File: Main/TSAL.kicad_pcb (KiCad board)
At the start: 2 copper layers, 140 x 70 mm, 81 parts, among them J1 Mini-SPOX, J2 Mini-SPOX, J3 Mini-Fit_Jr, J4 Mini-SPOX, J5 Mini-SPOX, J6 Jumper, J7 Jumper, Q1 IRLML2502, Q2 IRLML2502, Q3 IRLML2502, Q4 IRLML2502, Q5 IRF8721, U1 74HC08, U2 74HC08, U3 TLV70033, U4 LMC555, U5 LMR14030, U6 ZLDO1117G50, U7 TPS62205, U8 MAX40200AUK

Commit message: Main board: Rev B schematics design
major redesign of power delivery and backup
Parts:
- moved C1 28.3 mm to (187.0, 107.0)
- moved C10 28.3 mm to (118.0, 76.0)
- moved C11 28.3 mm to (129.0, 86.0)
- moved C12 28.3 mm to (120.5, 76.0)
- moved C13 28.3 mm to (199.0, 116.0)
- moved C14 28.3 mm to (144.0, 80.0)
- moved C15 28.3 mm to (205.0, 106.0)
- moved C16 28.3 mm to (201.0, 66.0)
- moved C17 28.3 mm to (201.0, 84.0)
- moved C18 28.3 mm to (183.0, 66.0)
- moved C19 28.3 mm to (183.0, 84.0)
- moved C2 28.3 mm to (101.0, 111.0)
- moved C20 28.3 mm to (165.0, 66.0)
- moved C21 28.3 mm to (165.0, 84.0)
- moved C22 28.3 mm to (163.5, 123.5)
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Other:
- net class Default: via_dia 0.8 -> 0.6; via_drill 0.4 -> 0.3
- board text removed: "GND"

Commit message: Added first rev of design of new TSAL main board
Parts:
- removed J6, J7: Jumper, Connector_PinHeader_2.54mm:PinHeader_1x02_P2.54mm_Vertical
- added C24: 10uF, Capacitor_SMD:C_1210_3225Metric, F.Cu at (177.8, 122.0)
- added C25: 0.1uF, Capacitor_SMD:C_0402_1005Metric, F.Cu at (153.1, 105.7)
- added C26: 10uF, Capacitor_SMD:C_0805_2012Metric, F.Cu at (155.5, 106.1)
- added C27: 100pF, Capacitor_SMD:C_0402_1005Metric, F.Cu at (150.8, 115.8)
- added C28: 0.1uF, Capacitor_SMD:C_0402_1005Metric, F.Cu at (159.2, 106.7)
- added C29: 1nF, Capacitor_SMD:C_0402_1005Metric, F.Cu at (152.7, 116.4)
- added C30: 100uF, Capacitor_SMD:C_1210_3225Metric, F.Cu at (177.4, 117.4)
- added C31: 100uF, Capacitor_SMD:C_1210_3225Metric, F.Cu at (177.4, 113.9)
- added C32: 100uF, Capacitor_SMD:C_1210_3225Metric, F.Cu at (177.4, 110.4)
- added C33: 200F, Capacitor_THT:CP_Radial_D30.0mm_P10.00mm_SnapIn, F.Cu at (152.0, 90.0)
- added C34: 200F, Capacitor_THT:CP_Radial_D30.0mm_P10.00mm_SnapIn, F.Cu at (183.0, 90.0)
- added C35: 0.1uF, Capacitor_SMD:C_0402_1005Metric, F.Cu at (149.0, 110.6)
- added C36: 200F, Capacitor_THT:CP_Radial_D30.0mm_P10.00mm_SnapIn, F.Cu at (121.0, 80.0)
- added C37: 200F, Capacitor_THT:CP_Radial_D30.0mm_P10.00mm_SnapIn, F.Cu at (90.0, 80.0)
- added C38: 0.1uF, Capacitor_SMD:C_0402_1005Metric, F.Cu at (145.2, 117.8)
- added C39: 1nF, Capacitor_SMD:C_0402_1005Metric, F.Cu at (154.0, 116.5)
- added C40: 0.1uF, Capacitor_SMD:C_0402_1005Metric, F.Cu at (132.4, 104.8)
- added C41: 0.1uF, Capacitor_SMD:C_0402_1005Metric, F.Cu at (106.4, 107.0)
- added C42: 1nF, Capacitor_SMD:C_0402_1005Metric, F.Cu at (141.0, 108.0)
- added C43: 0.1uF, Capacitor_SMD:C_0402_1005Metric, F.Cu at (117.3, 106.6)
- added C44: 1nF, Capacitor_SMD:C_0402_1005Metric, F.Cu at (139.0, 120.2)
- added C8: 10uF, Capacitor_SMD:C_1210_3225Metric, F.Cu at (129.6, 127.0)
- added L3: 2.2uH, Inductor_SMD:L_Bourns-SRN8040_8x8.15mm, F.Cu at (154.0, 122.5)
- added L4: 3.3uH, Inductor_SMD:L_Bourns_SRP1245A, F.Cu at (167.2, 108.2)
- added Q10: NPN, Package_TO_SOT_SMD:SOT-23, F.Cu at (147.5, 118.0)
- added Q11: MJD122, Package_TO_SOT_SMD:TO-252-2, F.Cu at (105.8, 100.8)
- added Q12: PNP, Package_TO_SOT_SMD:SOT-23, F.Cu at (146.5, 112.0)
- added Q6: BSC0904NSI, Package_TO_SOT_SMD:TDSON-8-1, F.Cu at (162.8, 123.5)
- added Q7: BSC0902NSI, Package_TO_SOT_SMD:TDSON-8-1, F.Cu at (178.5, 104.8)
- added Q8: BSC0902NSI, Package_TO_SOT_SMD:TDSON-8-1, F.Cu at (162.8, 117.8)
- added Q9: MJD122, Package_TO_SOT_SMD:TO-252-2, F.Cu at (136.8, 100.5)
- added R20: 10k, Resistor_SMD:R_0402_1005Metric, F.Cu at (117.8, 111.2)
- added R21: 10k, Resistor_SMD:R_0402_1005Metric, F.Cu at (119.8, 111.2)
- added R22: 10k, Resistor_SMD:R_0402_1005Metric, F.Cu at (118.8, 111.2)
- added R23: 47k, Resistor_SMD:R_0402_1005Metric, F.Cu at (150.8, 117.0)
- added R24: 0, project:Trace_0.4mmx0.8mm, F.Cu at (158.0, 109.9)
- added R25: 0, project:Trace_0.4mmx0.8mm, F.Cu at (158.0, 111.8)
- added R26: 10k, Resistor_SMD:R_0402_1005Metric, F.Cu at (124.2, 108.0)
- added R27: 15k, Resistor_SMD:R_0805_2012Metric, F.Cu at (147.5, 115.0)
- added R28: 68k, Resistor_SMD:R_0805_2012Metric, F.Cu at (159.5, 103.8)
- added R29: 10k, Resistor_SMD:R_0402_1005Metric, F.Cu at (120.8, 111.2)
- added R30: 56k, Resistor_SMD:R_0805_2012Metric, F.Cu at (156.5, 116.5)
- added R31: 0.006, Resistor_SMD:R_2512_6332Metric, F.Cu at (170.8, 117.2)
- added R32: 10k, Resistor_SMD:R_0402_1005Metric, F.Cu at (145.0, 115.5)
- added R33: 47k, Resistor_SMD:R_0402_1005Metric, F.Cu at (144.2, 117.8)
- added R34: 12k, Resistor_SMD:R_0805_2012Metric, F.Cu at (157.5, 103.8)
- added R35: 10k, Resistor_SMD:R_0402_1005Metric, F.Cu at (122.8, 111.2)
- added R36: 10k, Resistor_SMD:R_0402_1005Metric, F.Cu at (121.8, 111.2)
- added R37: 1k, Resistor_SMD:R_0402_1005Metric, F.Cu at (131.9, 103.3)
- added R38: 47k, Resistor_SMD:R_0402_1005Metric, F.Cu at (119.7, 101.0)
- added R39: 100k, Resistor_SMD:R_0402_1005Metric, F.Cu at (131.4, 104.8)
- added R40: 1k, Resistor_SMD:R_0402_1005Metric, F.Cu at (124.2, 104.0)
- added R41: 10k, Resistor_SMD:R_0402_1005Metric, F.Cu at (144.0, 111.0)
- added R42: 1k, Resistor_SMD:R_0402_1005Metric, F.Cu at (144.0, 113.2)
- added R43: 1k, Resistor_SMD:R_0402_1005Metric, F.Cu at (104.9, 107.5)
- added R44: 47k, Resistor_SMD:R_0402_1005Metric, F.Cu at (121.7, 101.0)
- added R45: 15k, Resistor_SMD:R_0805_2012Metric, F.Cu at (141.5, 113.2)
- added R46: 100k, Resistor_SMD:R_0402_1005Metric, F.Cu at (106.4, 108.0)
- added R47: 1k, Resistor_SMD:R_0402_1005Metric, F.Cu at (117.3, 104.6)
- added R48: 10k, Resistor_SMD:R_0805_2012Metric, F.Cu at (138.8, 110.2)
- added R49: 10k, Resistor_SMD:R_0805_2012Metric, F.Cu at (139.5, 115.2)
- added R50: 15k, Resistor_SMD:R_0805_2012Metric, F.Cu at (136.8, 116.0)
- added TP10: ~, TestPoint:TestPoint_Loop_D2.50mm_Drill1.0mm, F.Cu at (92.7, 104.8)
- added TP11: ~, TestPoint:TestPoint_Loop_D2.50mm_Drill1.0mm, F.Cu at (131.6, 108.0)
- added TP12: ~, TestPoint:TestPoint_Loop_D2.50mm_Drill1.0mm, F.Cu at (99.7, 104.8)
- added TP8: ~, TestPoint:TestPoint_Loop_D2.50mm_Drill1.0mm, F.Cu at (185.5, 103.8)
- added TP9: ~, TestPoint:TestPoint_Loop_D2.50mm_Drill1.0mm, F.Cu at (105.8, 73.8)
- added U10: TLV431, Package_TO_SOT_SMD:SOT-23, F.Cu at (141.5, 110.2)
- added U11: TLV431, Package_TO_SOT_SMD:SOT-23, F.Cu at (139.5, 118.0)
- added U9: LM25117, Package_SO:ETSSOP-20-1EP_4.4x6.5mm_P0.65mm_EP3x4.2mm, F.Cu at (154.0, 111.5)
- added ZZ1: ~, project:Trace_0.2mmx0.6mm, F.Cu at (142.7, 123.9)
- added ZZ2: ~, project:Trace_0.2mmx0.6mm, F.Cu at (145.1, 124.0)
- added ZZ3: ~, project:Trace_1mmx2mm, F.Cu at (141.6, 140.9)
- added ZZ4: ~, project:Trace_0.2mmx0.6mm, F.Cu at (117.3, 111.8)
- added ZZ5: ~, project:Trace_0.2mmx0.6mm, F.Cu at (157.8, 113.8)
- added ZZ6: ~, project:Trace_0.2mmx0.6mm, F.Cu at (120.7, 112.1)
- added ZZ7: ~, project:Trace_0.2mmx0.6mm, F.Cu at (157.0, 112.8)
- added ZZ8: ~, project:Trace_0.4mmx0.8mm, F.Cu at (152.0, 111.8)
- added ZZ9: ~, project:Trace_0.2mmx0.6mm, F.Cu at (122.3, 111.7)
- C1, C15, C4: value 10u -> 0.1uF; footprint Capacitor_SMD:C_0805_2012Metric_Pad1.15x1.40mm_HandSolder -> Capacitor_SMD:C_0402_1005Metric
- C10, C13, C14: value 10u -> 10uF; footprint Capacitor_SMD:C_0805_2012Metric_Pad1.15x1.40mm_HandSolder -> Capacitor_SMD:C_0805_2012Metric
- C11, C12: value 100n -> 10uF; footprint Capacitor_SMD:C_0805_2012Metric_Pad1.15x1.40mm_HandSolder -> Capacitor_SMD:C_0805_2012Metric
- C16, C17: value 35 -> 0.1uF; footprint Capacitor_THT:CP_Radial_D16.0mm_P7.50mm -> Capacitor_SMD:C_0402_1005Metric
- C18, C19: value 35 -> 220uF; footprint Capacitor_THT:CP_Radial_D16.0mm_P7.50mm -> Capacitor_SMD:CP_Elec_8x10.5
- C2, C3, C6: value 100n -> 0.1uF; footprint Capacitor_SMD:C_0805_2012Metric_Pad1.15x1.40mm_HandSolder -> Capacitor_SMD:C_0402_1005Metric
- C20, C21: value DNP -> 0.1uF; footprint Capacitor_THT:CP_Radial_D16.0mm_P7.50mm -> Capacitor_SMD:C_0402_1005Metric
- C22, C23: value 10u -> 10uF; footprint Capacitor_SMD:C_0805_2012Metric_Pad1.15x1.40mm_HandSolder -> Capacitor_SMD:C_1210_3225Metric
- C5: value 100n -> 2.2uF; footprint Capacitor_SMD:C_0805_2012Metric_Pad1.15x1.40mm_HandSolder -> Capacitor_SMD:C_0805_2012Metric
- C7: value 2.2u -> 10uF; footprint Capacitor_SMD:C_0805_2012Metric_Pad1.15x1.40mm_HandSolder -> Capacitor_SMD:C_1210_3225Metric
- C9: value 100u -> 10uF; footprint Capacitor_THT:CP_Radial_D5.0mm_P2.50mm -> Capacitor_SMD:C_0805_2012Metric
- D1: value SMF4L15A -> ~; footprint project:D_SOD-123_HandSolder -> Diode_SMD:D_SOD-123
- D2: value FSV1045V -> SMF4L15A; footprint project:TO-277A_HandSolder -> Diode_SMD:D_SOD-123
- D3: value S1A -> ~; footprint Diode_SMD:D_SMA_Handsoldering -> Diode_SMD:D_SOD-323
- F1: value 1A -> 6A; footprint Fuse:Fuseholder_Cylinder-5x20mm_Schurter_0031_8201_Horizontal_Open -> footprints_archive_old_design:Fuseholder_Littelfuse_Nano2_154x
- F2: value 3A -> 1A; footprint Fuse:Fuseholder_Cylinder-5x20mm_Schurter_0031_8201_Horizontal_Open -> footprints_archive_old_design:Fuseholder_Littelfuse_Nano2_154x
- J1: value Mini-SPOX -> Micro-Fit; footprint Connector_Molex:Molex_SPOX_5267-03A_1x03_P2.50mm_Vertical -> Connector_Molex:Molex_Micro-Fit_3.0_43045-0412_2x02_P3.00mm_Vertical
- J2: footprint Connector_Molex:Molex_SPOX_5267-06A_1x06_P2.50mm_Vertical -> Connector_Molex:Molex_SPOX_5267-03A_1x03_P2.50mm_Vertical
- J3: value Mini-Fit_Jr -> Mini-SPOX; footprint Connector_Molex:Molex_Mini-Fit_Jr_5566-02A_2x01_P4.20mm_Vertical -> Connector_Molex:Molex_SPOX_5267-04A_1x04_P2.50mm_Vertical
- J4: footprint Connector_Molex:Molex_SPOX_5267-04A_1x04_P2.50mm_Vertical -> Connector_Molex:Molex_SPOX_5267-06A_1x06_P2.50mm_Vertical
- JP1: value Jumper -> 0; footprint Jumper:SolderJumper-2_P1.3mm_Open_Pad1.0x1.5mm -> Resistor_SMD:R_0402_1005Metric
- L1: value 15u -> 1.5uH; footprint project:104CDMCCDS -> Inductor_SMD:L_Bourns-SRN4018
- L2: value 10u -> 4.7uH; footprint project:CDRH62B -> Inductor_SMD:L_Bourns-SRN4018
- Q1, Q2, Q3, Q4: footprint Package_TO_SOT_SMD:SOT-23_Handsoldering -> Package_TO_SOT_SMD:SOT-23
- Q5: value IRF8721 -> IRLML2502; footprint Package_SO:SOIC-8_3.9x4.9mm_P1.27mm -> Package_TO_SOT_SMD:SOT-23
- R1, R2, R6, R7, R8: footprint Resistor_SMD:R_0805_2012Metric_Pad1.15x1.40mm_HandSolder -> Resistor_SMD:R_0402_1005Metric
- R10: value 130k -> 100k; footprint Resistor_SMD:R_0805_2012Metric_Pad1.15x1.40mm_HandSolder -> Resistor_SMD:R_0402_1005Metric
- R11: value 1k -> 100k; footprint Resistor_SMD:R_0805_2012Metric_Pad1.15x1.40mm_HandSolder -> Resistor_SMD:R_0402_1005Metric
- R12: value 4.7 -> 0.006; footprint Resistor_THT:R_Axial_DIN0516_L15.5mm_D5.0mm_P20.32mm_Horizontal -> Resistor_SMD:R_2512_6332Metric
- R13: value 820k -> 56k; footprint Resistor_SMD:R_0805_2012Metric_Pad1.15x1.40mm_HandSolder -> Resistor_SMD:R_0805_2012Metric
- R14, R16: value 100k -> 10k; footprint Resistor_SMD:R_0805_2012Metric_Pad1.15x1.40mm_HandSolder -> Resistor_SMD:R_0805_2012Metric
- R15: value 100k -> 56k; footprint Resistor_SMD:R_0805_2012Metric_Pad1.15x1.40mm_HandSolder -> Resistor_SMD:R_0805_2012Metric
- R17: value 100k -> 68k; footprint Resistor_SMD:R_0805_2012Metric_Pad1.15x1.40mm_HandSolder -> Resistor_SMD:R_0805_2012Metric; moved to B.Cu
- R18: value 100k -> 10k; footprint Resistor_SMD:R_0805_2012Metric_Pad1.15x1.40mm_HandSolder -> Resistor_SMD:R_0402_1005Metric
- R19: value 100k -> 10k; footprint Resistor_SMD:R_0805_2012Metric_Pad1.15x1.40mm_HandSolder -> Resistor_SMD:R_0805_2012Metric; moved to B.Cu
- R3: value 22k -> 10k; footprint Resistor_SMD:R_0805_2012Metric_Pad1.15x1.40mm_HandSolder -> Resistor_SMD:R_0805_2012Metric
- R4: value 1k -> 10k; footprint Resistor_SMD:R_0805_2012Metric_Pad1.15x1.40mm_HandSolder -> Resistor_SMD:R_0402_1005Metric
- R5: value 22k -> 100k; footprint Resistor_SMD:R_0805_2012Metric_Pad1.15x1.40mm_HandSolder -> Resistor_SMD:R_0805_2012Metric
- R9: value 22k -> 100k; footprint Resistor_SMD:R_0805_2012Metric_Pad1.15x1.40mm_HandSolder -> Resistor_SMD:R_0402_1005Metric
- TP1: value TP_Timer_En -> ~; footprint TestPoint:TestPoint_THTPad_D2.0mm_Drill1.0mm -> TestPoint:TestPoint_Loop_D2.50mm_Drill1.0mm
- TP2: value TP_RLED_Ctrl -> ~; footprint TestPoint:TestPoint_THTPad_D2.0mm_Drill1.0mm -> TestPoint:TestPoint_Loop_D2.50mm_Drill1.0mm
- TP3: value TP_VCC -> ~; footprint TestPoint:TestPoint_THTPad_D2.0mm_Drill1.0mm -> TestPoint:TestPoint_Loop_D2.50mm_Drill1.0mm
- TP4: value TP_2V5 -> ~; footprint TestPoint:TestPoint_THTPad_D2.0mm_Drill1.0mm -> TestPoint:TestPoint_Loop_D2.50mm_Drill1.0mm
- TP5: value TP_Vcap -> ~; footprint TestPoint:TestPoint_THTPad_D2.0mm_Drill1.0mm -> TestPoint:TestPoint_Loop_D2.50mm_Drill1.0mm
- TP6: value TP_Vmid -> ~; footprint TestPoint:TestPoint_THTPad_D2.0mm_Drill1.0mm -> TestPoint:TestPoint_Loop_D2.50mm_Drill1.0mm
- TP7: value TP_GND -> ~; footprint TestPoint:TestPoint_THTPad_D2.0mm_Drill1.0mm -> TestPoint:TestPoint_Loop_D2.50mm_Drill1.0mm
- U1, U2: footprint Package_SO:SOIC-14_3.9x8.7mm_P1.27mm -> Package_SO:TSSOP-14_4.4x5mm_P0.65mm
- U3: value TLV70033 -> LMC555; footprint Package_TO_SOT_SMD:SOT-23-5_HandSoldering -> Package_SO:TSSOP-8_3x3mm_P0.65mm
- U4: value LMC555 -> TPS562200; footprint Package_SO:SOIC-8_3.9x4.9mm_P1.27mm -> Package_TO_SOT_SMD:SOT-23-6
- U5: value LMR14030 -> TPS63020; footprint Package_SO:SOIC-8-1EP_3.9x4.9mm_P1.27mm_EP2.41x3.3mm -> project:TPS63020
- U6: value ZLDO1117G50 -> MAX40200AUK; footprint Package_TO_SOT_SMD:SOT-223-3_TabPin2 -> Package_TO_SOT_SMD:SOT-23-5
- U7: value TPS62205 -> INA180A3; footprint Package_TO_SOT_SMD:SOT-23-5_HandSoldering -> Package_TO_SOT_SMD:SOT-23-5
- U8: value MAX40200AUK -> TLV9104; footprint Package_TO_SOT_SMD:SOT-23-5_HandSoldering -> Package_SO:TSSOP-14_4.4x5mm_P0.65mm
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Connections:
- C10 pad 1: /Power/VIN_F -> +5V
- C10 pad 2: GND -> GNDPWR
- C11 pad 2: GND -> GNDPWR
- C12 pad 1: Net-(C12-Pad1) -> Net-(C11-Pad1)
- C12 pad 2: Net-(C12-Pad2) -> GNDPWR
- C13 pad 1: /Power/VIN_F -> Net-(C13-Pad1)
- C13 pad 2: GND -> GNDPWR
- C14 pad 1: Net-(C14-Pad1) -> Net-(C13-Pad1)
- C14 pad 2: GND -> GNDPWR
- C15 pad 2: GND -> GNDPWR
- C16 pad 1: /Power/Vcap -> /Power/VCAP2
- C16 pad 2: Net-(C16-Pad2) -> GNDPWR
- C17 pad 1: Net-(C16-Pad2) -> Net-(C11-Pad1)
- C17 pad 2: GND -> GNDPWR
- C18 pad 1: /Power/Vcap -> /Power/V_IN
- C18 pad 2: Net-(C16-Pad2) -> GNDPWR
- C19 pad 1: Net-(C16-Pad2) -> Net-(C19-Pad1)
- C19 pad 2: GND -> GNDPWR
- C20 pad 1: /Power/Vcap -> +5V
- C20 pad 2: Net-(C16-Pad2) -> GNDA
- C21 pad 1: Net-(C16-Pad2) -> /Power/V_IN
- C21 pad 2: GND -> GNDPWR
- C22 pad 1: VCC -> Net-(C19-Pad1)
- C22 pad 2: GND -> GNDPWR
- C23 pad 1: +2V5 -> Net-(C19-Pad1)
- C23 pad 2: GND -> GNDPWR
- C4 pad 1: /TS_Inact_Out -> Net-(C4-Pad1)
- C5 pad 1: VCC -> Net-(C5-Pad1)
- C6 pad 2: GND -> Net-(C6-Pad2)
- C7 pad 1: Net-(C7-Pad1) -> /Power/V_IN
- C7 pad 2: GND -> GNDPWR
- C9 pad 1: /Power/VIN_F -> +5V
- C9 pad 2: GND -> GNDPWR
- D1 pad 1: /Power/VIN_F -> Net-(C11-Pad1)
- D1 pad 2: GND -> +5V
- D2 pad 1: GND -> Net-(D2-Pad1)
- D2 pad 2: GND -> GNDPWR
- D3 pad 1: VCC -> /Power/HB
- D3 pad 2: Net-(C15-Pad1) -> /Power/BUCK_VCC
- F1 pad 1: /VCC_F -> Net-(D2-Pad1)
- F1 pad 2: VCC -> VIN
- F2 pad 1: /Power/VIN_F -> VCC
- F2 pad 2: VIN -> Net-(C13-Pad1)
- J1 pad 1: /VCC_F -> GNDPWR
- J1 pad 2: /Sense_1 -> VIN
- J1 pad 3: GND -> GNDPWR
- J2 pad 1: /VCC_F -> GND
- J2 pad 2: GND -> /Sense_1
- J2 pad 3: /Sense_2 -> VCC
- J3 pad 1: VIN -> VCC
- J3 pad 2: GND -> /RLED-
- J4 pad 1: +2V5 -> /AUX_1
- J4 pad 2: /RLED- -> /AUX_2
- J4 pad 3: +2V5 -> /AUX_3
- J4 pad 4: /GLED- -> VCC
- J5 pad 1: /TS_Inact_Out -> VCC
- J5 pad 2: GND -> /Dash_LED-
- JP1 pad 1: Net-(J7-Pad1) -> /Power/BUCK_VCC
- JP1 pad 2: /Power/Vcap -> /Power/DEMB
- L1 pad 1: Net-(C12-Pad2) -> Net-(L1-Pad1)
- L1 pad 2: Net-(C14-Pad1) -> Net-(L1-Pad2)
- L2 pad 1: Net-(L2-Pad1) -> Net-(C6-Pad1)
- L2 pad 2: +2V5 -> +5V
- Q2 pad 3: Net-(Q1-Pad2) -> /RLED-
- Q3 pad 1: Net-(Q2-Pad1) -> Net-(Q3-Pad1)
- Q3 pad 3: Net-(Q3-Pad3) -> Net-(Q1-Pad2)
- Q4 pad 1: Net-(Q4-Pad1) -> Net-(Q3-Pad1)
- Q4 pad 3: /RLED- -> Net-(Q4-Pad3)
- Q5 pad 1: Net-(C14-Pad1) -> Net-(Q3-Pad1)
- Q5 pad 2: Net-(C14-Pad1) -> GND
- Q5 pad 3: Net-(C14-Pad1) -> /Dash_LED-
- R10 pad 1: Net-(C14-Pad1) -> /Sense_2
- R10 pad 2: Net-(R10-Pad2) -> GND
- R11 pad 1: Net-(C15-Pad1) -> /Sense_1
- R12 pad 1: /Power/Vcap -> Net-(D2-Pad1)
- R12 pad 2: Net-(J6-Pad1) -> /Power/V_IN
- R13 pad 1: /Power/VIN_F -> +5V
- R14 pad 2: GND -> GNDPWR
- R15 pad 1: /Sense_1 -> Net-(C13-Pad1)
- R15 pad 2: GND -> Net-(R15-Pad2)
- R16 pad 1: /Sense_2 -> Net-(R15-Pad2)
- R16 pad 2: GND -> GNDPWR
- R17 pad 1: /AUX_1 -> /Power/V_IN
- R17 pad 2: GND -> /Power/UVLO
- R18 pad 1: /AUX_2 -> Net-(R18-Pad1)
- R18 pad 2: GND -> /Power/CAP_D2
- R19 pad 1: /AUX_3 -> /Power/UVLO
- R19 pad 2: GND -> GNDA
- R3 pad 2: Net-(Q3-Pad3) -> Net-(R3-Pad2)
- R4 pad 1: Net-(R4-Pad1) -> VCC
- R4 pad 2: Net-(Q3-Pad3) -> Net-(Q4-Pad3)
- R5 pad 1: VCC -> Net-(R3-Pad2)
- R5 pad 2: Net-(R5-Pad2) -> Net-(C5-Pad1)
- R6 pad 1: Net-(R5-Pad2) -> Net-(Q3-Pad1)
- R6 pad 2: Net-(C7-Pad1) -> GND
- R7 pad 1: Net-(Q4-Pad1) -> /AUX_3
- R8 pad 1: Net-(R8-Pad1) -> /AUX_2
- R9 pad 1: Net-(R10-Pad2) -> /AUX_1
- TP1 pad 1: Net-(R4-Pad1) -> /Power/V_IN
- TP2 pad 1: Net-(Q4-Pad1) -> GNDPWR
- TP3 pad 1: VCC -> Net-(C11-Pad1)
- TP4 pad 1: +2V5 -> VCC
- TP5 pad 1: /Power/Vcap -> GND
- TP6 pad 1: Net-(C16-Pad2) -> /Power/I_SENSE
- TP7 pad 1: GND -> /Power/CM
- U2 pad 11: Net-(Q2-Pad1) -> Net-(Q3-Pad1)
- U3 pad 1: VCC -> GND
- U3 pad 2: GND -> Net-(C5-Pad1)
- U3 pad 4: (no net) -> Net-(Q4-Pad3)
- U3 pad 5: /TS_Inact_Out -> Net-(C4-Pad1)
- U4 pad 1: GND -> GNDPWR
- U4 pad 2: Net-(C7-Pad1) -> Net-(C6-Pad1)
- U4 pad 3: Net-(Q4-Pad1) -> /Power/V_IN
- U4 pad 4: Net-(R4-Pad1) -> Net-(R13-Pad2)
- U4 pad 5: Net-(C6-Pad1) -> /Power/V_IN
- U4 pad 6: Net-(C7-Pad1) -> Net-(C6-Pad2)
- U5 pad 1: Net-(C12-Pad1) -> Net-(C15-Pad1)
- U5 pad 2: /Power/VIN_F -> GNDPWR
- U5 pad 3: Net-(R13-Pad2) -> Net-(R15-Pad2)
- U5 pad 4: Net-(R8-Pad1) -> Net-(C13-Pad1)
- U5 pad 5: Net-(R10-Pad2) -> (no net)
- U5 pad 6: Net-(C11-Pad1) -> Net-(L1-Pad2)
- U5 pad 7: GND -> Net-(L1-Pad2)
- U5 pad 8: Net-(C12-Pad2) -> Net-(L1-Pad1)
- U5 pad 9: GND -> Net-(L1-Pad1)
- U6 pad 1: GND -> /Power/VCAP2
- U6 pad 2: Net-(C15-Pad1) -> GNDPWR
- U6 pad 3: /Power/VIN_F -> /Power/VCAP2
- U7 pad 1: VCC -> /Power/I_SENSE
- U7 pad 2: GND -> GNDA
- U7 pad 3: VCC -> /Power/IN_CS+
- U7 pad 4: +2V5 -> /Power/IN_CS-
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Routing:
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- added copper zone on B.Cu, net GNDPWR
- added copper zone on F.Cu, net GNDPWR
- removed copper zone on F.Cu, net /Power/VIN_F
- removed copper zone on B.Cu, net /Power/Vcap
- removed copper zone on F.Cu, net /Power/Vcap
- removed copper zone on B.Cu, net GND
- removed copper zone on F.Cu, net GND
- removed copper zone on F.Cu, net Net-(C12-Pad2)
- removed copper zone on F.Cu, net Net-(C14-Pad1)
- removed copper zone on B.Cu, net Net-(C16-Pad2)
- removed copper zone on F.Cu, net Net-(C16-Pad2)
- removed copper zone on F.Cu, net Net-(J7-Pad1)
- removed copper zone on B.Cu, net VIN
- removed copper zone on F.Cu, net VIN
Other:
- board size 140 x 70 mm -> 140 x 75 mm
- board text added: "5V"
- board text added: "AUX_1"
- board text added: "AUX_2"
- board text added: "AUX_3"
- board text added: "BLNC1"
- board text added: "BLNC2"
- board text added: "Buck-conv."
- board text added: "CM"
- board text added: "Dash LEDs"
- board text added: "Dash_LED-"
- board text added: "GLED-"
- board text added: "GND"
- board text added: "GNDPWR"
- board text added: "GND_CAP"
- board text added: "I_IN"
- board text added: "RLED-"
- board text added: "Rev. B 24/02/2021"
- board text added: "Sense_1"
- board text added: "Sense_2"
- board text added: "TSAL LEDs"
- board text added: "VCAP1"
- board text added: "VCAP2"
- board text added: "VCC"
- board text added: "V_IN"
- board text removed: "LEDs"
- board text removed: "Rev. A"
- board text removed: "Status Out"

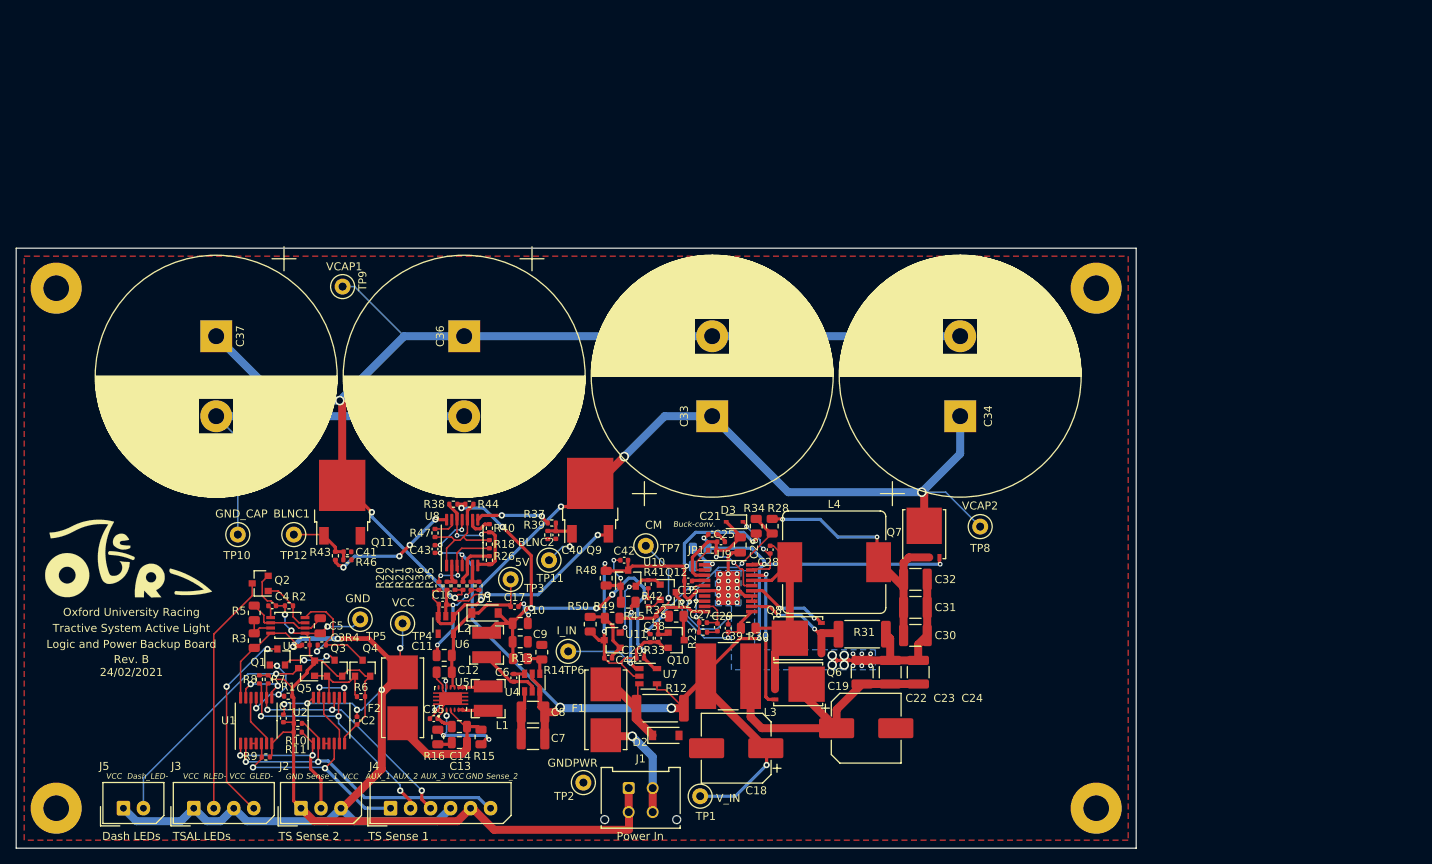
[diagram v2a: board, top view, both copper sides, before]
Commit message: Main: optimized layout
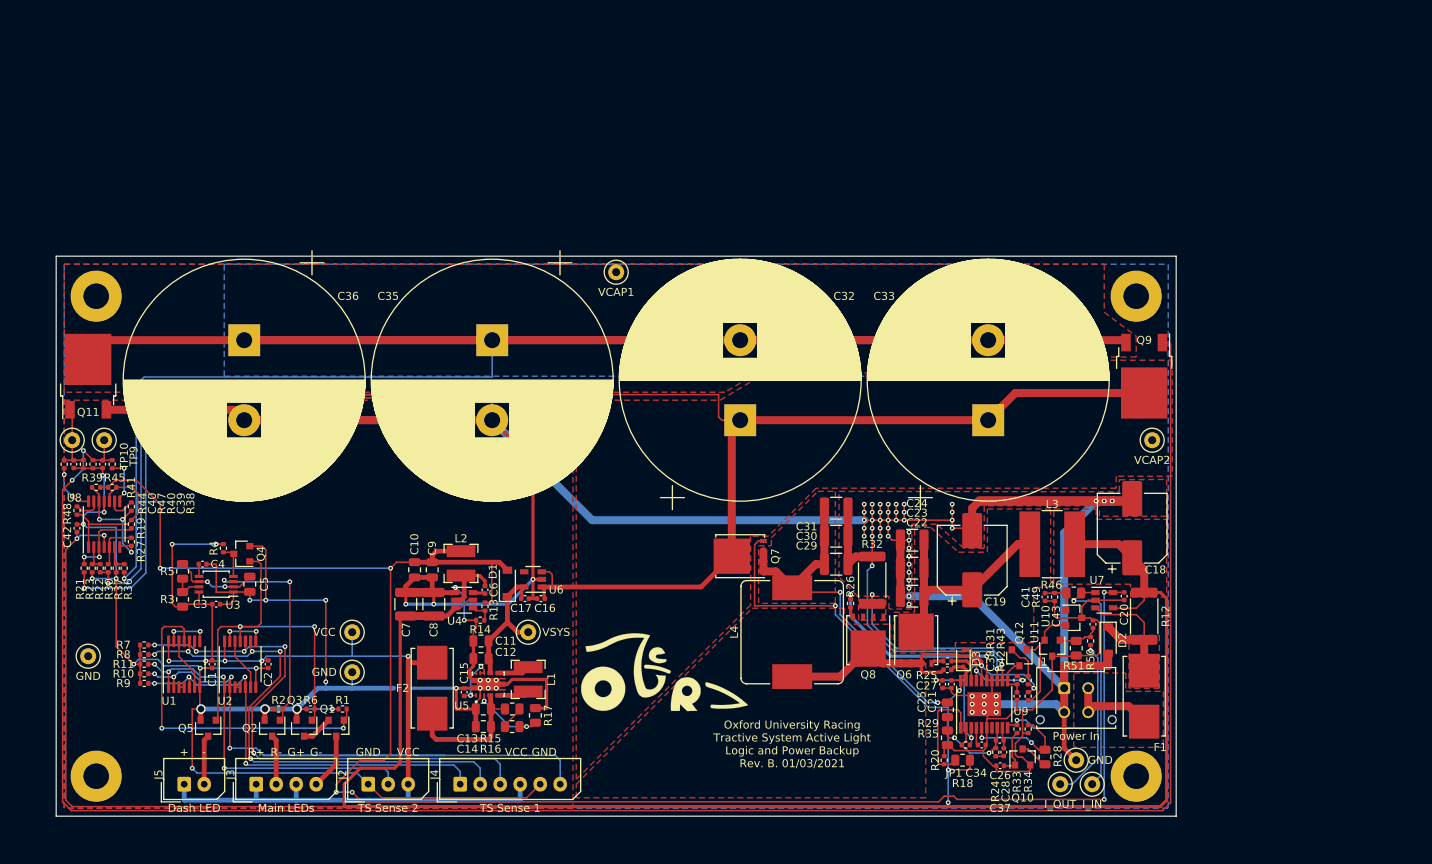
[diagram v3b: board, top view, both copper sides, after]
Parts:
- removed the C33 at (152.0, 90.0)
- removed the C35 at (149.0, 110.6)
- removed the C39 at (154.0, 116.5)
- removed C44: 1nF, Capacitor_SMD:C_0402_1005Metric
- removed the R38 at (119.7, 101.0)
- removed the R40 at (124.2, 104.0)
- removed the R44 at (121.7, 101.0)
- removed the R47 at (117.3, 104.6)
- removed the TP10 at (92.7, 104.8)
- removed the TP9 at (105.8, 73.8)
- removed ZZ9: ~, project:Trace_0.2mmx0.6mm
- added C34: 0.1uF, Capacitor_SMD:C_0402_1005Metric, F.Cu at (185.7, 131.1)
- added C36: 200F, Capacitor_THT:CP_Radial_D30.0mm_P10.00mm_SnapIn, F.Cu at (93.5, 80.5)
- added C40: 0.1uF, Capacitor_SMD:C_0402_1005Metric, F.Cu at (72.2, 96.0)
- added R37: 10k, Resistor_SMD:R_0402_1005Metric, F.Cu at (77.5, 109.0)
- added R39: 47k, Resistor_SMD:R_0402_1005Metric, F.Cu at (75.0, 98.9)
- added R43: 1k, Resistor_SMD:R_0402_1005Metric, F.Cu at (191.5, 123.0)
- added R46: 15k, Resistor_SMD:R_0805_2012Metric, F.Cu at (197.2, 112.1)
- added R51: 15k, Resistor_SMD:R_0805_2012Metric, F.Cu at (197.5, 119.0)
- added TP11: ~, TestPoint:TestPoint_Loop_D2.50mm_Drill1.0mm, F.Cu at (74.0, 120.0)
- C21, C25: value 0.1uF -> 1uF
- C26: value 10uF -> 100pF; footprint Capacitor_SMD:C_0805_2012Metric -> Capacitor_SMD:C_0402_1005Metric
- C27: value 100pF -> 1uF
- C28, C38, C41, C43: value 0.1uF -> 1nF
- C29: value 1nF -> 100uF; footprint Capacitor_SMD:C_0402_1005Metric -> Capacitor_SMD:C_1210_3225Metric
- C32: value 100uF -> 200F; footprint Capacitor_SMD:C_1210_3225Metric -> Capacitor_THT:CP_Radial_D30.0mm_P10.00mm_SnapIn
- C37: value 200F -> 0.1uF; footprint Capacitor_THT:CP_Radial_D30.0mm_P10.00mm_SnapIn -> Capacitor_SMD:C_0402_1005Metric
- C42: value 1nF -> 0.1uF
- R13, R14, R49: footprint Resistor_SMD:R_0805_2012Metric -> Resistor_SMD:R_0402_1005Metric
- R15: value 56k -> 1M
- R16: value 10k -> 100k
- R17: value 68k -> 180k; moved to F.Cu
- R18, R29: value 10k -> 68k; footprint Resistor_SMD:R_0402_1005Metric -> Resistor_SMD:R_0805_2012Metric
- R19: footprint Resistor_SMD:R_0805_2012Metric -> Resistor_SMD:R_0402_1005Metric; moved to F.Cu
- R23, R33: value 47k -> 10k
- R24: value 0 -> 47k; footprint project:Trace_0.4mmx0.8mm -> Resistor_SMD:R_0402_1005Metric
- R25: footprint project:Trace_0.4mmx0.8mm -> Resistor_SMD:R_0402_1005Metric
- R26: value 10k -> 0
- R27, R50: value 15k -> 10k; footprint Resistor_SMD:R_0805_2012Metric -> Resistor_SMD:R_0402_1005Metric
- R28: value 68k -> 15k
- R30: value 56k -> 10k; footprint Resistor_SMD:R_0805_2012Metric -> Resistor_SMD:R_0402_1005Metric
- R31: value 0.006 -> 56k; footprint Resistor_SMD:R_2512_6332Metric -> Resistor_SMD:R_0402_1005Metric
- R32: value 10k -> 0.006; footprint Resistor_SMD:R_0402_1005Metric -> Resistor_SMD:R_2512_6332Metric
- R34: value 12k -> 47k; footprint Resistor_SMD:R_0805_2012Metric -> Resistor_SMD:R_0402_1005Metric
- R35: value 10k -> 12k; footprint Resistor_SMD:R_0402_1005Metric -> Resistor_SMD:R_0805_2012Metric
- R41: value 10k -> 1k
- R42: value 1k -> 10k
- R45: value 15k -> 47k; footprint Resistor_SMD:R_0805_2012Metric -> Resistor_SMD:R_0402_1005Metric
- R48: value 10k -> 1k; footprint Resistor_SMD:R_0805_2012Metric -> Resistor_SMD:R_0402_1005Metric
- ZZ3: footprint project:Trace_1mmx2mm -> project:Trace_0.2mmx0.6mm
- ZZ5: moved to B.Cu
- ZZ8: footprint project:Trace_0.4mmx0.8mm -> project:Trace_0.2mmx0.6mm
- moved C37 111.7 mm to (188.0, 133.7), turned to 180 degrees
- moved TP5 91.2 mm to (197.5, 133.0), turned to 0 degrees
- moved TP4 88.5 mm to (199.5, 136.0), turned to 0 degrees
- moved C41 87.4 mm to (193.6, 112.6), turned to 270 degrees
- moved C43 82.8 mm to (199.6, 116.0)
- moved R30 80.4 mm to (76.5, 109.0), turned to 90 degrees
- moved R23 76.8 mm to (74.5, 109.0), turned to 90 degrees
- moved R19 71.3 mm to (79.4, 103.5), turned to 90 degrees
- moved Q9 71.0 mm to (206.0, 85.0), turned to 270 degrees
- moved R27 68.7 mm to (79.4, 105.7), turned to 270 degrees
- moved C42 68.5 mm to (72.6, 104.0), turned to 90 degrees
- moved G*** 68.5 mm to (146.0, 122.0)
- moved F1 67.3 mm to (206.0, 125.0)
- moved R20 66.8 mm to (181.0, 133.0)
- moved R48 66.7 mm to (72.6, 101.8), turned to 270 degrees
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- renumbered C34 to C33, C36 to C35, C40 to C39, R37 to R38, R39 to R40, R43 to R44, R46 to R47, TP12 to TP10, TP11 to TP9
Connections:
- net Net-(C19-Pad1) renamed /Power/SW_IN
- C10 pad 2: GNDPWR -> GND
- C11 pad 2: GNDPWR -> GND
- C12 pad 2: GNDPWR -> GND
- C13 pad 2: GNDPWR -> GND
- C14 pad 2: GNDPWR -> GND
- C15 pad 2: GNDPWR -> GND
- C16 pad 2: GNDPWR -> GND
- C17 pad 2: GNDPWR -> GND
- C18 pad 2: GNDPWR -> GND
- C19 pad 2: GNDPWR -> GND
- C21 pad 2: GNDPWR -> GND
- C22 pad 2: GNDPWR -> GND
- C23 pad 2: GNDPWR -> GND
- C24 pad 2: GNDPWR -> GND
- C25 pad 2: GNDPWR -> GND
- C26 pad 1: /Power/BUCK_VCC -> /Power/COMP
- C26 pad 2: GNDPWR -> /Power/FB
- C27 pad 1: /Power/COMP -> /Power/HB
- C27 pad 2: /Power/FB -> /Power/SW
- C28 pad 1: /Power/HB -> /Power/COMP
- C28 pad 2: /Power/SW -> Net-(C28-Pad2)
- C29 pad 1: /Power/COMP -> /Power/V_CHARGE
- C29 pad 2: Net-(C29-Pad2) -> GND
- C30 pad 2: GNDPWR -> GND
- C31 pad 2: GNDPWR -> GND
- C32 pad 1: /Power/V_CHARGE -> /Power/VCAP2
- C32 pad 2: GNDPWR -> /Power/VCAP1
- C35 pad 2: GNDPWR -> GND
- C37 pad 1: /Power/VCAP1 -> Net-(C37-Pad1)
- C37 pad 2: GNDPWR -> GNDA
- C38 pad 1: Net-(C38-Pad1) -> /Power/RAMP
- C39 pad 2: GNDPWR -> GND
- C41 pad 1: /Power/BAL_CTRL1 -> Net-(C41-Pad1)
- C41 pad 2: GNDPWR -> GNDA
- C42 pad 1: Net-(C42-Pad1) -> /Power/V_IN
- C42 pad 2: GNDA -> GND
- C43 pad 1: /Power/V_IN -> Net-(C43-Pad1)
- C43 pad 2: GNDPWR -> GNDA
- C7 pad 2: GNDPWR -> GND
- C8 pad 2: GNDPWR -> GND
- C9 pad 2: GNDPWR -> GND
- D2 pad 2: GNDPWR -> GND
- J1 pad 1: GNDPWR -> GND
- J1 pad 3: GNDPWR -> GND
- Q10 pad 1: Net-(C38-Pad1) -> Net-(C37-Pad1)
- Q11 pad 3: GNDPWR -> GND
- R14 pad 2: GNDPWR -> GND
- R16 pad 2: GNDPWR -> Net-(R16-Pad2)
- R17 pad 1: /Power/V_IN -> Net-(R16-Pad2)
- R17 pad 2: /Power/UVLO -> GND
- R18 pad 1: Net-(R18-Pad1) -> /Power/V_IN
- R18 pad 2: /Power/CAP_D2 -> /Power/UVLO
- R19 pad 1: /Power/UVLO -> Net-(R19-Pad1)
- R19 pad 2: GNDA -> /Power/CAP_D2
- R20 pad 1: /Power/CAP_V2 -> /Power/UVLO
- R20 pad 2: Net-(R18-Pad1) -> GNDA
- R21 pad 1: /Power/CAP_V1 -> Net-(R21-Pad1)
- R21 pad 2: Net-(R21-Pad2) -> Net-(R19-Pad1)
- R22 pad 1: GNDPWR -> Net-(R22-Pad1)
- R22 pad 2: Net-(R21-Pad2) -> Net-(R22-Pad2)
- R23 pad 1: Net-(C29-Pad2) -> GND
- R23 pad 2: /Power/FB -> Net-(R22-Pad2)
- R24 pad 1: Net-(Q6-Pad4) -> Net-(C28-Pad2)
- R24 pad 2: /Power/HO -> /Power/FB
- R25 pad 1: Net-(Q8-Pad4) -> Net-(Q6-Pad4)
- R25 pad 2: /Power/LO -> /Power/HO
- R26 pad 1: Net-(R26-Pad1) -> Net-(Q8-Pad4)
- R26 pad 2: /Power/CAP_D1 -> /Power/LO
- R27 pad 1: /Power/RT -> Net-(R27-Pad1)
- R27 pad 2: Net-(Q10-Pad3) -> /Power/CAP_D1
- R28 pad 1: /Power/V_CHARGE -> /Power/RT
- R28 pad 2: /Power/FB -> Net-(Q10-Pad3)
- R29 pad 1: /Power/CAP_V1 -> /Power/V_CHARGE
- R29 pad 2: Net-(R26-Pad1) -> /Power/FB
- R30 pad 1: /Power/SW -> Net-(R22-Pad1)
- R30 pad 2: /Power/RAMP -> Net-(R27-Pad1)
- R31 pad 1: Net-(Q8-Pad1) -> /Power/SW
- R31 pad 2: GNDPWR -> /Power/RAMP
- R32 pad 1: /Power/CM -> Net-(Q8-Pad1)
- R32 pad 2: Net-(C38-Pad1) -> GND
- R33 pad 1: /Power/RT -> /Power/CM
- R33 pad 2: GNDA -> Net-(C37-Pad1)
- R34 pad 1: /Power/FB -> /Power/RT
- R35 pad 1: /Power/CAP_V0 -> /Power/FB
- R35 pad 2: Net-(R35-Pad2) -> GNDA
- R36 pad 1: GNDPWR -> Net-(R36-Pad1)
- R36 pad 2: Net-(R35-Pad2) -> Net-(R36-Pad2)
- R40 pad 1: GNDPWR -> GND
- R41 pad 1: +5V -> Net-(R41-Pad1)
- R41 pad 2: Net-(Q12-Pad1) -> /Power/CAP_D1
- R42 pad 1: +5V -> /Power/BUCK_VCC
- R42 pad 2: Net-(Q12-Pad2) -> Net-(Q12-Pad1)
- R45 pad 1: /Power/I_SENSE -> /Power/CAP_D2
- R45 pad 2: Net-(C42-Pad1) -> +5V
- R47 pad 1: GNDPWR -> GND
- R48 pad 1: Net-(C42-Pad1) -> Net-(R48-Pad1)
- R48 pad 2: GNDA -> /Power/CAP_D2
- R49 pad 1: /Power/CM -> Net-(C41-Pad1)
- R49 pad 2: Net-(C44-Pad1) -> GNDA
- R50 pad 1: Net-(C44-Pad1) -> /Power/CM
- R50 pad 2: GNDA -> Net-(C43-Pad1)
- TP1 pad 1: /Power/V_IN -> Net-(C11-Pad1)
- TP2 pad 1: GNDPWR -> VCC
- TP3 pad 1: Net-(C11-Pad1) -> GND
- TP4 pad 1: VCC -> /Power/I_IN
- TP6 pad 1: /Power/I_SENSE -> /Power/CM
- TP7 pad 1: /Power/CM -> /Power/VCAP2
- TP8 pad 1: /Power/VCAP2 -> /Power/VCAP1
- U10 pad 1: Net-(C42-Pad1) -> Net-(C41-Pad1)
- U11 pad 1: Net-(C44-Pad1) -> Net-(C43-Pad1)
- U4 pad 1: GNDPWR -> GND
- U5 pad 13: GNDPWR -> Net-(C15-Pad1)
- U5 pad 14: Net-(U5-Pad14) -> (no net)
- U5 pad 15: GNDPWR -> GND
- U5 pad 2: GNDPWR -> GND
- U5 pad 3: Net-(R15-Pad2) -> Net-(R16-Pad2)
- U5 pad 5: (no net) -> Net-(C13-Pad1)
- U6 pad 2: GNDPWR -> GND
- U6 pad 4: Net-(U6-Pad4) -> (no net)
- U7 pad 1: /Power/I_SENSE -> /Power/I_IN
- U8 pad 11: GNDPWR -> GND
- U8 pad 13: Net-(R47-Pad1) -> Net-(R48-Pad1)
- U8 pad 2: Net-(R21-Pad2) -> Net-(R22-Pad2)
- U8 pad 3: Net-(R18-Pad1) -> Net-(R19-Pad1)
- U8 pad 5: Net-(R26-Pad1) -> Net-(R27-Pad1)
- U8 pad 6: Net-(R35-Pad2) -> Net-(R36-Pad2)
- U8 pad 9: Net-(R40-Pad1) -> Net-(R41-Pad1)
- U9 pad : (no net) -> GND
- U9 pad 14: GNDPWR -> GND
- U9 pad 21: GNDPWR -> GND
- U9 pad 4: Net-(C35-Pad1) -> /Power/SS
- U9 pad 7: Net-(U9-Pad7) -> (no net)
- ZZ3 pad 1: GNDPWR -> /Power/VCAP2
- ZZ3 pad 2: GND -> Net-(R21-Pad1)
- ZZ4 pad 1: /Power/VCAP2 -> /Power/CS
- ZZ4 pad 2: /Power/CAP_V2 -> Net-(Q8-Pad1)
- ZZ5 pad 1: /Power/CS -> /Power/VCAP1
- ZZ5 pad 2: Net-(Q8-Pad1) -> Net-(R22-Pad1)
- ZZ6 pad 1: /Power/VCAP1 -> /Power/CSG
- ZZ6 pad 2: /Power/CAP_V1 -> GND
- ZZ7 pad 1: /Power/CSG -> GNDA
- ZZ7 pad 2: GNDPWR -> GND
- ZZ8 pad 1: GNDA -> GND
- ZZ8 pad 2: GNDPWR -> Net-(R36-Pad1)
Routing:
- net GND: track 115.9 -> 641.8 mm, vias 3 -> 81
- net /Power/BAL_CTRL2: track 9.21 -> 249.5 mm, vias 1 -> 2
- net /Power/V_IN: track 143.2 -> 320.7 mm, vias 9 -> 6
- net +5V: track 63.3 -> 229.6 mm, vias 7 -> 6
- net GNDPWR: track 140.4 -> 0.00 mm, vias 32 -> 0
- net Net-(R21-Pad1): track 0.00 -> 131.0 mm, vias 0 -> 2
- net Net-(R22-Pad1): track 0.00 -> 74.9 mm, vias 0 -> 1
- net Net-(R36-Pad1): track 0.00 -> 68.5 mm, vias 0 -> 2
- net /Power/VCAP1: track 167.7 -> 228.0 mm, vias 5 -> 0
- net /Sense_2: track 41.2 -> 90.4 mm, vias 2 -> 4
- net /AUX_3: track 31.2 -> 69.3 mm, vias 3 -> 5
- net Net-(Q3-Pad1): track 11.1 -> 49.1 mm, vias 0 -> 2
- net /AUX_2: track 31.5 -> 66.2 mm, vias 3 -> 5
- net Net-(Q1-Pad1): track 11.0 -> 42.3 mm, vias 3 -> 2
- net /Power/I_IN: track 0.00 -> 29.9 mm, vias 0 -> 1
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- added copper zone on F.Cu, net /Power/SW
- added copper zone on F.Cu, net /Power/SW_IN
- added copper zone on B.Cu, net /Power/VCAP1
- added copper zone on F.Cu, net /Power/VCAP1
- added copper zone on F.Cu, net /Power/VCAP2
- added copper zone on F.Cu, net /Power/V_CHARGE
- added copper zone on F.Cu, net /Power/V_IN
- added copper zone on B.Cu, net GND
- added copper zone on F.Cu, net GND
- added copper zone on F.Cu, net Net-(D2-Pad1)
- added copper zone on F.Cu, net Net-(Q8-Pad1)
- added copper zone on F.Cu, net VIN
- removed copper zone on B.Cu, net GNDPWR
- removed copper zone on F.Cu, net GNDPWR
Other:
- board size 140 x 75 mm -> 140 x 70 mm
- board text added: "+"
- board text added: "-"
- board text added: "Dash LED"
- board text added: "G+"
- board text added: "G-"
- board text added: "Main LEDs"
- board text added: "Oxford University Racing Tractive System Active Light Logic and Power Backup Rev. B. 01/03/2021"
- board text added: "R+"
- board text added: "R-"
- board text removed: "5V"
- board text removed: "AUX_1"
- board text removed: "AUX_2"
- board text removed: "AUX_3"
- board text removed: "BLNC1"
- board text removed: "BLNC2"
- board text removed: "Buck-conv."
- board text removed: "CM"
- board text removed: "Dash LEDs"
- board text removed: "Dash_LED-"
- board text removed: "GLED-"
- board text removed: "GNDPWR"
- board text removed: "GND_CAP"
- board text removed: "I_IN"
- board text removed: "Logic and Power Backup Board"
- board text removed: "Oxford University Racing"
- board text removed: "RLED-"
- board text removed: "Rev. B 24/02/2021"
- board text removed: "Sense_1"
- board text removed: "Sense_2"
- board text removed: "TSAL LEDs"
- board text removed: "Tractive System Active Light"
- board text removed: "VCAP1"
- board text removed: "VCAP2"
- board text removed: "V_IN"

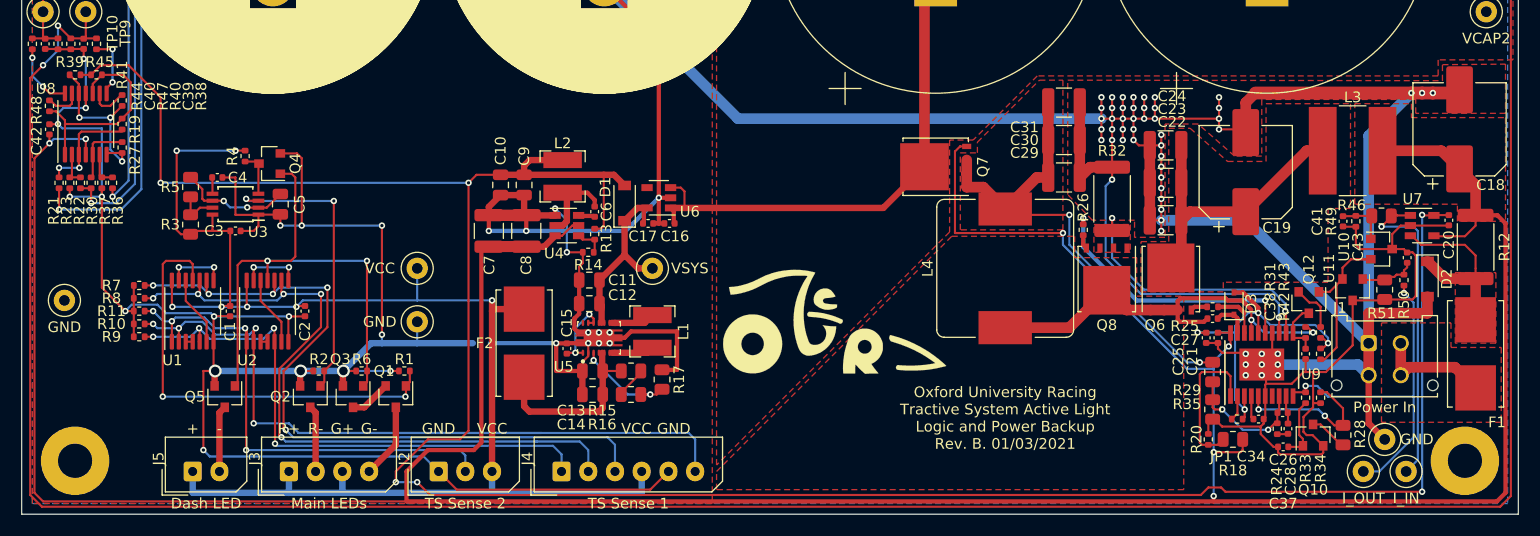
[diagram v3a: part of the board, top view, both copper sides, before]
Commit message: Main: update sot23-5/6 footprints
Bloody kicad libaries
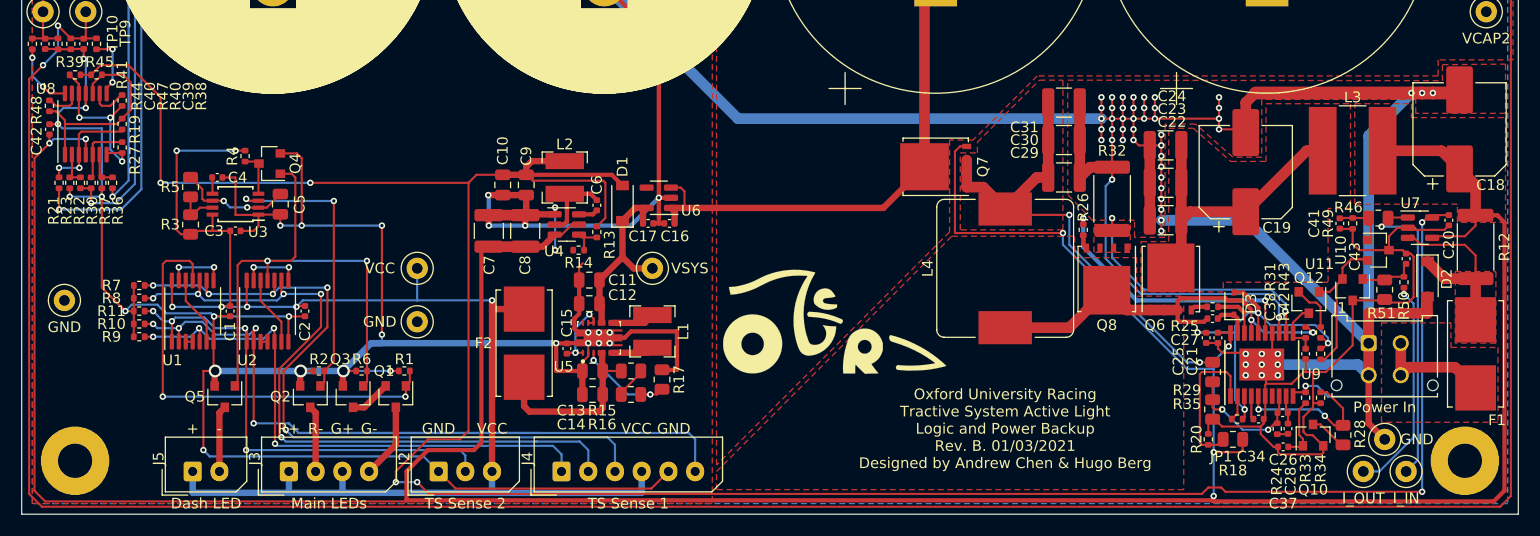
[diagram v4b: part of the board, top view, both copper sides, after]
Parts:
- F1, F2: footprint footprints_archive_old_design:Fuseholder_Littelfuse_Nano2_154x -> Fuse:Fuseholder_Littelfuse_Nano2_154x
- moved R14 0.92 mm to (122.1, 115.3)
- moved C6 0.63 mm to (123.8, 111.1)
- moved R49 0.36 mm to (194.5, 112.8)
- moved C41 0.36 mm to (193.3, 112.8)
- moved R46 0.36 mm to (196.9, 112.3)
- moved U10 0.32 mm to (196.9, 115.3)
- moved R13 0.28 mm to (123.8, 113.6)
- moved U7 0.28 mm to (200.8, 113.2)
- moved L2 0.22 mm to (120.8, 108.5)
- moved C10 0.20 mm to (115.0, 109.2)
- moved C9 0.20 mm to (117.2, 109.2)
- moved D1 0.20 mm to (126.2, 110.9)
- moved R50 0.20 mm to (199.3, 118.3)
- moved C43 0.14 mm to (199.5, 116.1)
- moved C8 0.10 mm to (117.1, 113.5)
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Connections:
- U9 pad : GND -> (no net)
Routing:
- net +5V: track 229.6 -> 235.7 mm
- net GND: track 641.8 -> 637.6 mm, vias 81 -> 82
- net /Power/V_IN: track 320.7 -> 317.0 mm
- net Net-(C6-Pad1): track 8.01 -> 7.35 mm
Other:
- board text added: "Oxford University Racing Tractive System Active Light Logic and Power Backup Rev. B. 01/03/2021 Designed by Andrew Chen & Hugo Berg"
- board text removed: "Oxford University Racing Tractive System Active Light Logic and Power Backup Rev. B. 01/03/2021"
